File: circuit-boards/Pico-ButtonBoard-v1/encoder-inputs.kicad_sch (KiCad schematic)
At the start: 22 parts, among them J601 ENC0, J602 ENC1, J603 ENC2, J604 ENC PWR

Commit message: Pico Button Board initial pcb checkin
Signed-off-by: Scott Berman <sgberman1@gmail.com>
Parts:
- renumbered J602 to J1, J604 to J17, J601 to J18, J603 to J2, R610 to R12, R611 to R13, R612 to R14, R616 to R15, R617 to R16, R618 to R17, R606 to R30, R605 to R31, R602 to R32, R604 to R50, R603 to R51, R601 to R52, R607 to R67, R608 to R68, R609 to R69, R613 to R70, R614 to R71, R615 to R72
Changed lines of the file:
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@@
 		(dnp no)
 		(fields_autoplaced yes)
-		(property "Reference" "J604"
+		(property "Reference" "J17"
 			(at 257.81 34.29 0)
 			(effects
@@
 			(project ""
 				(path "/644201a9-3a2f-4df3-9c93-2ae55394df4b/d0d9a62e-3d08-419e-af51-4493246764fe"
-					(reference "J604")
+					(reference "J17")
 					(unit 1)
 				)
@@
 		(on_board yes)
 		(dnp no)
-		(property "Reference" "R602"
+		(property "Reference" "R32"
 			(at 192.278 53.594 90)
 			(effects
@@
 			(project "Pico-ButtonBoard-v1"
 				(path "/644201a9-3a2f-4df3-9c93-2ae55394df4b/d0d9a62e-3d08-419e-af51-4493246764fe"
-					(reference "R602")
+					(reference "R32")
 					(unit 1)
 				)
@@
 		(on_board yes)
 		(dnp no)
-		(property "Reference" "R607"
+		(property "Reference" "R67"
 			(at 166.624 132.08 90)
 			(effects
@@
 			(project "Pico-ButtonBoard-v1"
 				(path "/644201a9-3a2f-4df3-9c93-2ae55394df4b/d0d9a62e-3d08-419e-af51-4493246764fe"
-					(reference "R607")
+					(reference "R67")
 					(unit 1)
 				)
@@
 		(on_board yes)
 		(dnp no)
-		(property "Reference" "R609"
+		(property "Reference" "R69"
 			(at 181.864 132.08 90)
 			(effects
@@
 			(project "Pico-ButtonBoard-v1"
 				(path "/644201a9-3a2f-4df3-9c93-2ae55394df4b/d0d9a62e-3d08-419e-af51-4493246764fe"
-					(reference "R609")
+					(reference "R69")
 					(unit 1)
 				)
@@
 		(dnp no)
 		(fields_autoplaced yes)
-		(property "Reference" "J601"
+		(property "Reference" "J18"
 			(at 153.67 48.26 0)
 			(effects
@@
 			(project ""
 				(path "/644201a9-3a2f-4df3-9c93-2ae55394df4b/d0d9a62e-3d08-419e-af51-4493246764fe"
-					(reference "J601")
+					(reference "J18")
 					(unit 1)
 				)
@@
 		(dnp no)
 		(fields_autoplaced yes)
-		(property "Reference" "J602"
+		(property "Reference" "J1"
 			(at 153.67 101.6 0)
 			(effects
@@
 			(project "Pico-ButtonBoard-v1"
 				(path "/644201a9-3a2f-4df3-9c93-2ae55394df4b/d0d9a62e-3d08-419e-af51-4493246764fe"
-					(reference "J602")
+					(reference "J1")
 					(unit 1)
 				)
@@
 		(on_board yes)
 		(dnp no)
-		(property "Reference" "R616"
+		(property "Reference" "R15"
 			(at 192.278 161.544 90)
 			(effects
@@
 			(project "Pico-ButtonBoard-v1"
 				(path "/644201a9-3a2f-4df3-9c93-2ae55394df4b/d0d9a62e-3d08-419e-af51-4493246764fe"
-					(reference "R616")
+					(reference "R15")
 					(unit 1)
 				)
@@
 		(on_board yes)
 		(dnp no)
-		(property "Reference" "R606"
+		(property "Reference" "R30"
 			(at 192.278 66.294 90)
 			(effects
@@
 			(project "Pico-ButtonBoard-v1"
 				(path "/644201a9-3a2f-4df3-9c93-2ae55394df4b/d0d9a62e-3d08-419e-af51-4493246764fe"
-					(reference "R606")
+					(reference "R30")
 					(unit 1)
 				)
@@
 		(on_board yes)
 		(dnp no)
-		(property "Reference" "R618"
+		(property "Reference" "R17"
 			(at 192.278 174.244 90)
 			(effects
@@
 			(project "Pico-ButtonBoard-v1"
 				(path "/644201a9-3a2f-4df3-9c93-2ae55394df4b/d0d9a62e-3d08-419e-af51-4493246764fe"
-					(reference "R618")
+					(reference "R17")
 					(unit 1)
 				)
@@
 		(dnp no)
 		(fields_autoplaced yes)
-		(property "Reference" "J603"
+		(property "Reference" "J2"
 			(at 153.67 156.21 0)
 			(effects
@@
 			(project "Pico-ButtonBoard-v1"
 				(path "/644201a9-3a2f-4df3-9c93-2ae55394df4b/d0d9a62e-3d08-419e-af51-4493246764fe"
-					(reference "J603")
+					(reference "J2")
 					(unit 1)
 				)
@@
 		(on_board yes)
 		(dnp no)
-		(property "Reference" "R614"
+		(property "Reference" "R71"
 			(at 174.244 186.69 90)
 			(effects
@@
 			(project "Pico-ButtonBoard-v1"
 				(path "/644201a9-3a2f-4df3-9c93-2ae55394df4b/d0d9a62e-3d08-419e-af51-4493246764fe"
-					(reference "R614")
+					(reference "R71")
 					(unit 1)
 				)
@@
 		(on_board yes)
 		(dnp no)
-		(property "Reference" "R612"
+		(property "Reference" "R14"
 			(at 192.278 119.634 90)
 			(effects
@@
 			(project "Pico-ButtonBoard-v1"
 				(path "/644201a9-3a2f-4df3-9c93-2ae55394df4b/d0d9a62e-3d08-419e-af51-4493246764fe"
-					(reference "R612")
+					(reference "R14")
 					(unit 1)
 				)
@@
 		(on_board yes)
 		(dnp no)
-		(property "Reference" "R611"
+		(property "Reference" "R13"
 			(at 192.278 113.284 90)
 			(effects
@@
 			(project "Pico-ButtonBoard-v1"
 				(path "/644201a9-3a2f-4df3-9c93-2ae55394df4b/d0d9a62e-3d08-419e-af51-4493246764fe"
-					(reference "R611")
+					(reference "R13")
 					(unit 1)
 				)
@@
 		(on_board yes)
 		(dnp no)
-		(property "Reference" "R605"
+		(property "Reference" "R31"
 			(at 192.278 59.944 90)
 			(effects
@@
 			(project "Pico-ButtonBoard-v1"
 				(path "/644201a9-3a2f-4df3-9c93-2ae55394df4b/d0d9a62e-3d08-419e-af51-4493246764fe"
-					(reference "R605")
+					(reference "R31")
 					(unit 1)
 				)
@@
 		(on_board yes)
 		(dnp no)
-		(property "Reference" "R617"
+		(property "Reference" "R16"
 			(at 192.278 167.894 90)
 			(effects
@@
 			(project "Pico-ButtonBoard-v1"
 				(path "/644201a9-3a2f-4df3-9c93-2ae55394df4b/d0d9a62e-3d08-419e-af51-4493246764fe"
-					(reference "R617")
+					(reference "R16")
 					(unit 1)
 				)
@@
 		(on_board yes)
 		(dnp no)
-		(property "Reference" "R608"
+		(property "Reference" "R68"
 			(at 174.244 132.08 90)
 			(effects
@@
 			(project "Pico-ButtonBoard-v1"
 				(path "/644201a9-3a2f-4df3-9c93-2ae55394df4b/d0d9a62e-3d08-419e-af51-4493246764fe"
-					(reference "R608")
+					(reference "R68")
 					(unit 1)
 				)
@@
 		(on_board yes)
 		(dnp no)
-		(property "Reference" "R610"
+		(property "Reference" "R12"
 			(at 192.278 106.934 90)
 			(effects
@@
 			(project "Pico-ButtonBoard-v1"
 				(path "/644201a9-3a2f-4df3-9c93-2ae55394df4b/d0d9a62e-3d08-419e-af51-4493246764fe"
-					(reference "R610")
+					(reference "R12")
 					(unit 1)
 				)
@@
 		(on_board yes)
 		(dnp no)
-		(property "Reference" "R615"
+		(property "Reference" "R72"
 			(at 181.864 186.69 90)
 			(effects
@@
 			(project "Pico-ButtonBoard-v1"
 				(path "/644201a9-3a2f-4df3-9c93-2ae55394df4b/d0d9a62e-3d08-419e-af51-4493246764fe"
-					(reference "R615")
+					(reference "R72")
 					(unit 1)
 				)
@@
 		(on_board yes)
 		(dnp no)
-		(property "Reference" "R613"
+		(property "Reference" "R70"
 			(at 166.624 186.69 90)
 			(effects
@@
 			(project "Pico-ButtonBoard-v1"
 				(path "/644201a9-3a2f-4df3-9c93-2ae55394df4b/d0d9a62e-3d08-419e-af51-4493246764fe"
-					(reference "R613")
+					(reference "R70")
 					(unit 1)
 				)
@@
 		(on_board yes)
 		(dnp no)
-		(property "Reference" "R604"
+		(property "Reference" "R50"
 			(at 181.864 78.74 90)
 			(effects
@@
 			(project "Pico-ButtonBoard-v1"
 				(path "/644201a9-3a2f-4df3-9c93-2ae55394df4b/d0d9a62e-3d08-419e-af51-4493246764fe"
-					(reference "R604")
+					(reference "R50")
 					(unit 1)
 				)
@@
 		(on_board yes)
 		(dnp no)
-		(property "Reference" "R601"
+		(property "Reference" "R52"
 			(at 166.624 78.74 90)
 			(effects
@@
 			(project "Pico-ButtonBoard-v1"
 				(path "/644201a9-3a2f-4df3-9c93-2ae55394df4b/d0d9a62e-3d08-419e-af51-4493246764fe"
-					(reference "R601")
+					(reference "R52")
 					(unit 1)
 				)
@@
 		(on_board yes)
 		(dnp no)
-		(property "Reference" "R603"
+		(property "Reference" "R51"
 			(at 174.244 78.74 90)
 			(effects
@@
 			(project "Pico-ButtonBoard-v1"
 				(path "/644201a9-3a2f-4df3-9c93-2ae55394df4b/d0d9a62e-3d08-419e-af51-4493246764fe"
-					(reference "R603")
+					(reference "R51")
 					(unit 1)
 				)

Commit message: Update Pico Button Board Layout
Signed-off-by: Scott Berman <sgberman1@gmail.com>
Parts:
- J17: DIST (none) -> Digikey; DIST P/N (none) -> 732-5316-ND; MFG (none) -> Würth Elektronik; MFG P/N (none) -> 61300311121; now in the parts list
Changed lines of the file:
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@@
 	(title_block
 		(title "Pico Button Board")
-		(date "2025-12-25")
+		(date "2025-12-28")
 		(rev "1")
 	)
@@
 		(unit 1)
 		(exclude_from_sim no)
-		(in_bom no)
+		(in_bom yes)
 		(on_board yes)
 		(dnp no)
@@
 			(at 257.81 43.18 0)
 			(effects
+				(font
+					(size 1.27 1.27)
+				)
+				(hide yes)
+			)
+		)
+		(property "MFG" "Würth Elektronik"
+			(at 257.81 43.18 0)
+			(effects
+				(font
+					(size 1.27 1.27)
+				)
+				(hide yes)
+			)
+		)
+		(property "MFG P/N" "61300311121"
+			(at 257.81 43.18 0)
+			(effects
+				(font
+					(size 1.27 1.27)
+				)
+				(hide yes)
+			)
+		)
+		(property "DIST" "Digikey"
+			(at 257.81 43.18 0)
+			(effects
+				(font
+					(size 1.27 1.27)
+				)
+				(hide yes)
+			)
+		)
+		(property "DIST P/N" "732-5316-ND"
+			(at 257.81 43.18 0)
+			(effects

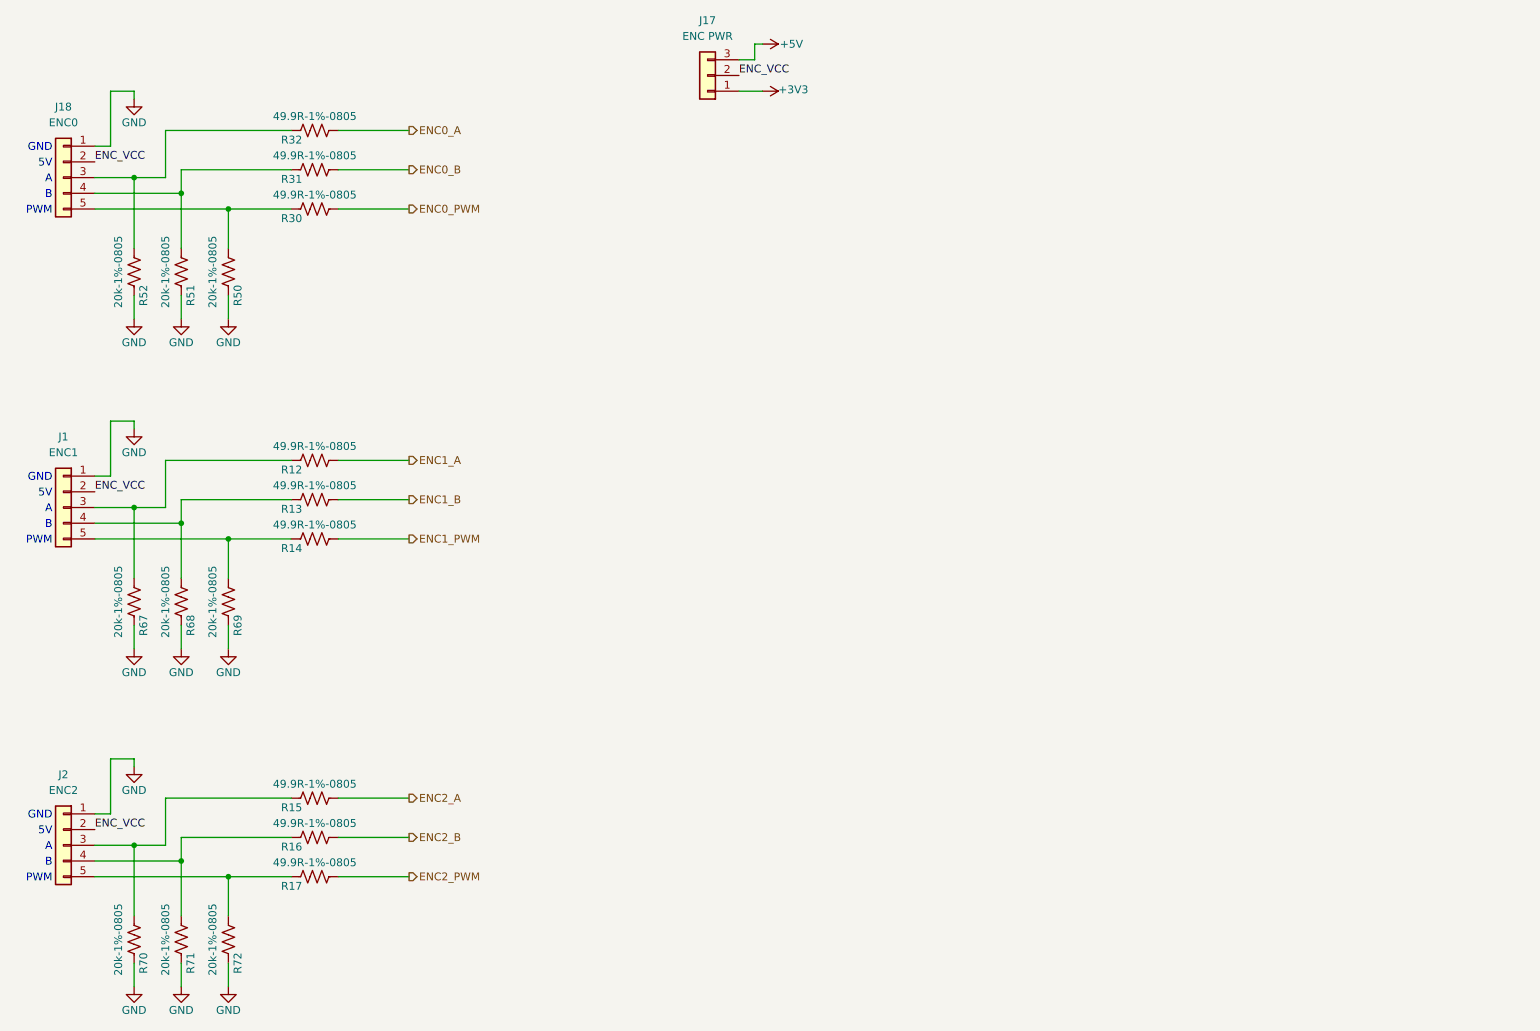
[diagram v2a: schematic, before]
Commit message: Changed button input circuit to use mux. Changed ADC3 to an external SPI ADC
Signed-off-by: Scott Berman <sgberman1@gmail.com>
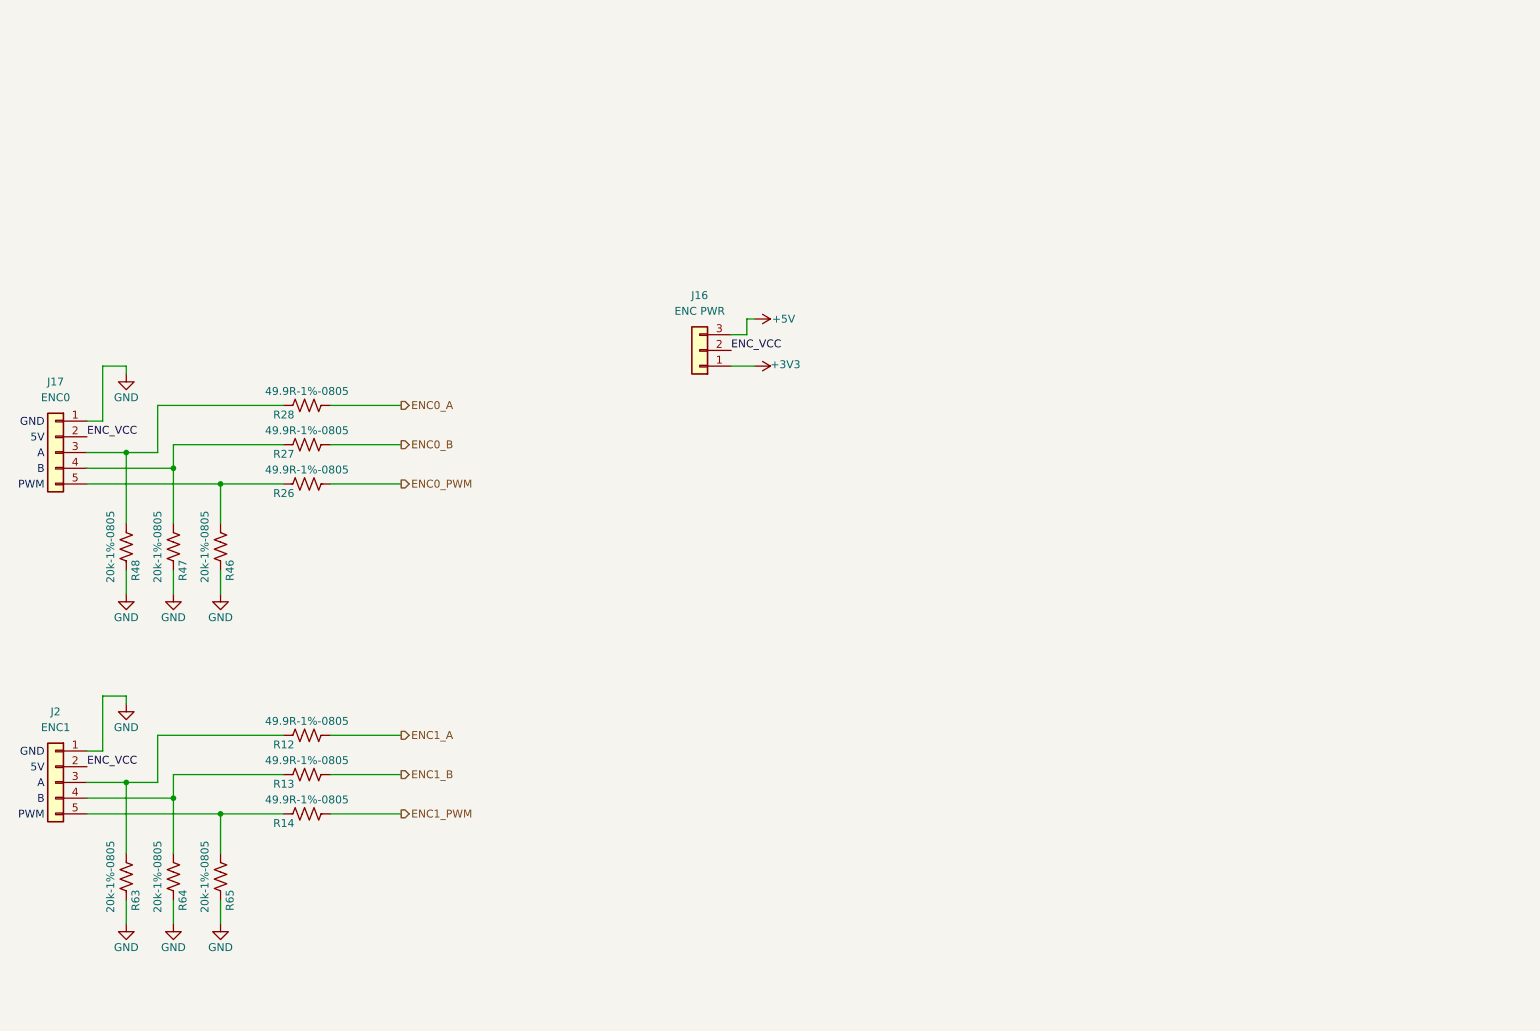
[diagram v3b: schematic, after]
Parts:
- removed J2: ENC2, Pico-ButtonBoard:Molex-70543-0039, symbol Connector_Generic:Conn_01x05
- removed R15, R16, R17: 49.9R-1%-0805, Resistor_SMD:R_0805_2012Metric_Pad1.20x1.40mm_HandSolder, symbol Device:R_US
- removed R70, R71, R72: 20k-1%-0805, Resistor_SMD:R_0805_2012Metric_Pad1.20x1.40mm_HandSolder, symbol Device:R_US
- renumbered J17 to J16, J18 to J17, J1 to J2, R30 to R26, R31 to R27, R32 to R28, R50 to R46, R51 to R47, R52 to R48, R67 to R63, R68 to R64, R69 to R65
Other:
- moved on the sheet: J16, J17, J2, R12, R13, R14, R26, R27, R28, R46, R47, R48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

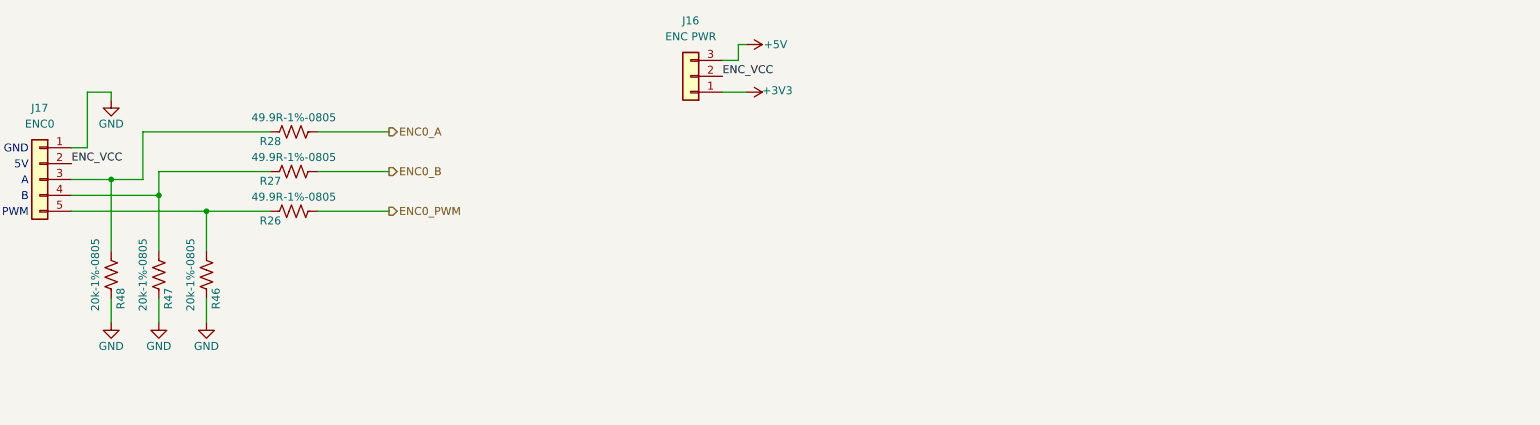
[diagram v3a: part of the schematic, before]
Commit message: Add power over CAN to supply joystick from button interfaces.
Signed-off-by: Scott Berman <sgberman1@gmail.com>
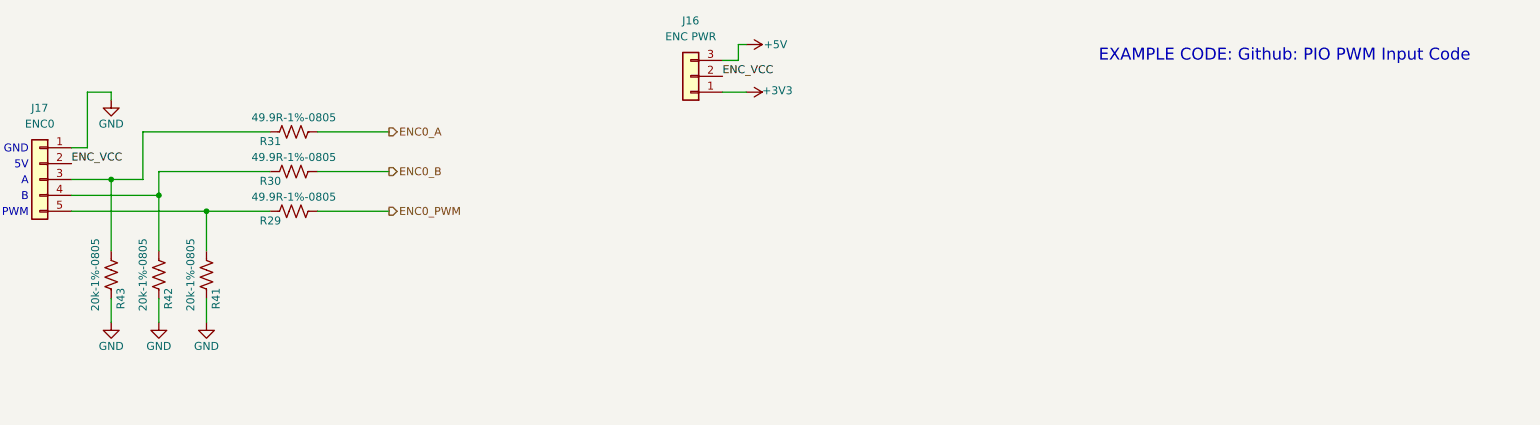
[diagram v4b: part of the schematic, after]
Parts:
- renumbered R26 to R29, R27 to R30, R28 to R31, R46 to R41, R47 to R42, R48 to R43
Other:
- note added: "EXAMPLE CODE: Github: PIO PWM Input Code"
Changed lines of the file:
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@@
 	(title_block
 		(title "Pico Button Board")
-		(date "2025-12-29")
+		(date "2025-12-30")
 		(rev "1")
 	)
@@
 			)
 			(justify right)
+		)
+	)
+	(text "EXAMPLE CODE: Github: PIO PWM Input Code"
+		(exclude_from_sim no)
+		(at 351.536 84.328 0)
+		(effects
+			(font
+				(size 1.905 1.905)
+			)
+			(href "https://github.com/GitJer/Some_RPI-Pico_stuff/tree/main/PwmIn")
 		)
 	)
@@
 		(on_board yes)
 		(dnp no)
-		(property "Reference" "R28"
+		(property "Reference" "R31"
 			(at 191.008 98.044 90)
 			(effects
@@
 			(project "Pico-ButtonBoard-v1"
 				(path "/644201a9-3a2f-4df3-9c93-2ae55394df4b/d0d9a62e-3d08-419e-af51-4493246764fe"
-					(reference "R28")
+					(reference "R31")
 					(unit 1)
 				)
@@
 		(on_board yes)
 		(dnp no)
-		(property "Reference" "R26"
+		(property "Reference" "R29"
 			(at 191.008 110.744 90)
 			(effects
@@
 			(project "Pico-ButtonBoard-v1"
 				(path "/644201a9-3a2f-4df3-9c93-2ae55394df4b/d0d9a62e-3d08-419e-af51-4493246764fe"
-					(reference "R26")
+					(reference "R29")
 					(unit 1)
 				)
@@
 		(on_board yes)
 		(dnp no)
-		(property "Reference" "R27"
+		(property "Reference" "R30"
 			(at 191.008 104.394 90)
 			(effects
@@
 			(project "Pico-ButtonBoard-v1"
 				(path "/644201a9-3a2f-4df3-9c93-2ae55394df4b/d0d9a62e-3d08-419e-af51-4493246764fe"
-					(reference "R27")
+					(reference "R30")
 					(unit 1)
 				)
@@
 		(on_board yes)
 		(dnp no)
-		(property "Reference" "R46"
+		(property "Reference" "R41"
 			(at 180.594 123.19 90)
 			(effects
@@
 			(project "Pico-ButtonBoard-v1"
 				(path "/644201a9-3a2f-4df3-9c93-2ae55394df4b/d0d9a62e-3d08-419e-af51-4493246764fe"
-					(reference "R46")
+					(reference "R41")
 					(unit 1)
 				)
@@
 		(on_board yes)
 		(dnp no)
-		(property "Reference" "R48"
+		(property "Reference" "R43"
 			(at 165.354 123.19 90)
 			(effects
@@
 			(project "Pico-ButtonBoard-v1"
 				(path "/644201a9-3a2f-4df3-9c93-2ae55394df4b/d0d9a62e-3d08-419e-af51-4493246764fe"
-					(reference "R48")
+					(reference "R43")
 					(unit 1)
 				)
@@
 		(on_board yes)
 		(dnp no)
-		(property "Reference" "R47"
+		(property "Reference" "R42"
 			(at 172.974 123.19 90)
 			(effects
@@
 			(project "Pico-ButtonBoard-v1"
 				(path "/644201a9-3a2f-4df3-9c93-2ae55394df4b/d0d9a62e-3d08-419e-af51-4493246764fe"
-					(reference "R47")
+					(reference "R42")
 					(unit 1)
 				)
